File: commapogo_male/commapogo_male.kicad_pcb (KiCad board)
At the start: 2 copper layers, 40.6 x 22.2 mm, 6 parts, among them J1 Conn_02x07_Row_Letter_Last, J2 Conn_02x12_Row_Letter_Last

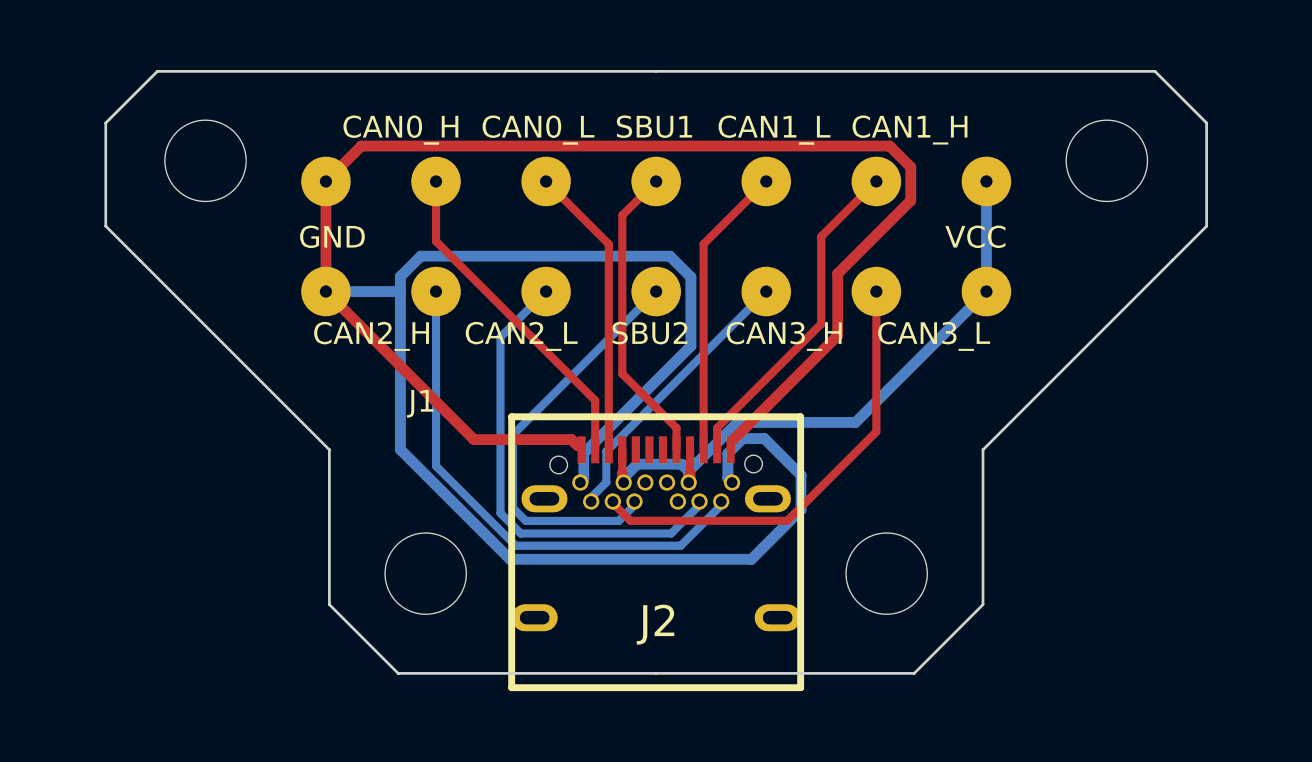
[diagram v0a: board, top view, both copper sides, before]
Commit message: rework usb-c footprint for jlcpcb
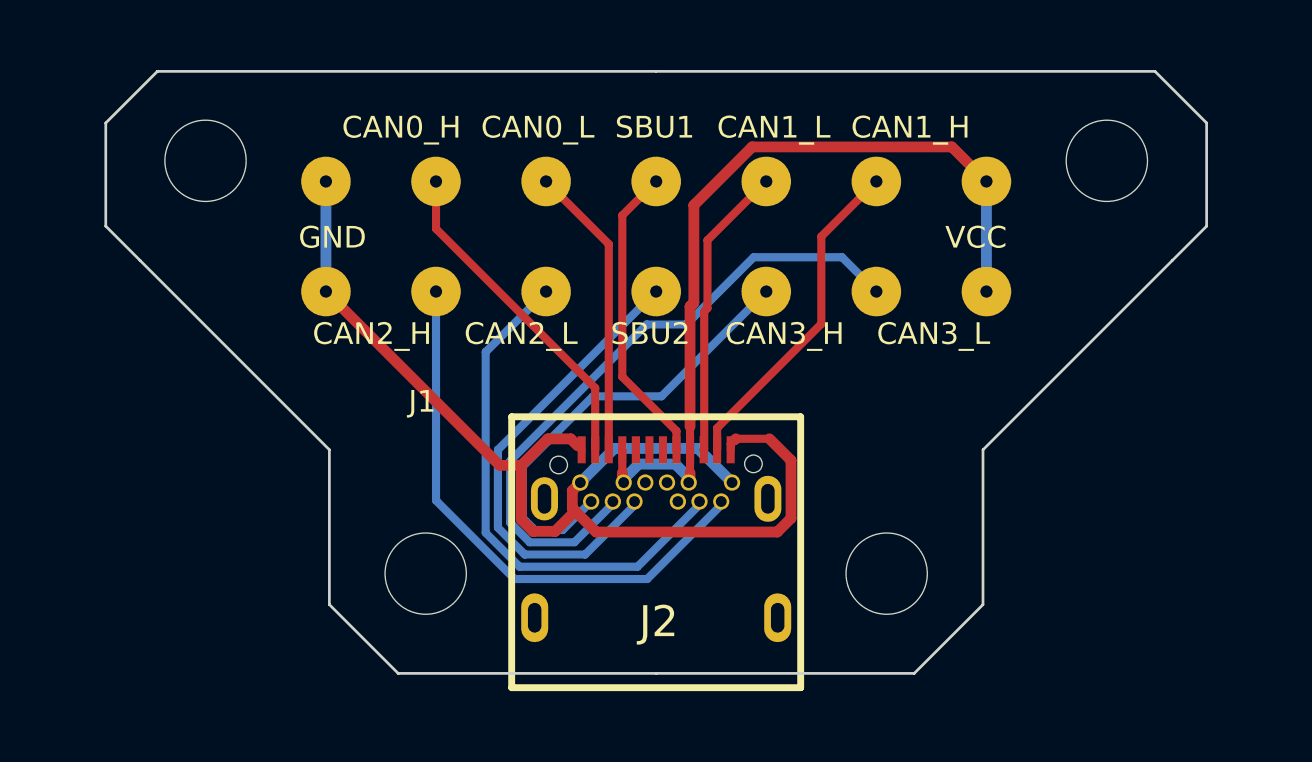
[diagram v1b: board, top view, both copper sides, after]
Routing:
- net GND: track 104.5 -> 42.6 mm
- net /CAN3_L: track 16.6 -> 24.2 mm
- net +12V: track 23.6 -> 31.0 mm
- net /CAN3_H: track 10.4 -> 16.7 mm
- net /SBU2: track 15.2 -> 17.5 mm
- net /CAN2_L: track 17.1 -> 19.3 mm
- net /CAN2_H: track 18.9 -> 20.7 mm

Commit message: revised PCB
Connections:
- J1 pad 10: /CAN2_L -> /CAN3_L
- J1 pad 12: /CAN3_H -> /CAN2_L
- J1 pad 13: /CAN3_L -> /CAN2_H
- J1 pad 7: +12V -> GND
- J1 pad 8: GND -> +12V
- J1 pad 9: /CAN2_H -> /CAN3_H
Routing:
- net /CAN3_L: track 24.2 -> 8.77 mm
- net /SBU2: track 17.5 -> 32.3 mm
- net GND: track 42.6 -> 29.6 mm, vias 0 -> 2
- net /CAN2_L: track 19.3 -> 8.77 mm
- net /CAN2_H: track 20.7 -> 11.0 mm
- net +12V: track 31.0 -> 38.7 mm
- net /CAN3_H: track 16.7 -> 12.7 mm
- added copper zone on B.Cu, net GND
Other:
- board text added: "GND"
- board text added: "VCC"

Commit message: rework pcb design
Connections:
- J2 pad 1: (no net) -> GND
- J2 pad 2: (no net) -> GND
- J2 pad 3: (no net) -> GND
- J2 pad 4: (no net) -> GND
- J2 pad B7: unconnected-(J2-Pin_7b-PadB7) -> /SBU2
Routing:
- net /SBU2: track 32.3 -> 8.21 mm
- net GND: track 29.6 -> 5.61 mm, vias 2 -> 0
- net +12V: track 38.7 -> 35.8 mm
- net /CAN3_H: track 12.7 -> 10.2 mm
- net /CAN2_H: track 11.0 -> 12.7 mm
- net /SBU1: track 11.2 -> 11.6 mm, vias 0 -> 1
- net /CAN1_L: track 10.9 -> 11.1 mm, vias 0 -> 1
- net /CAN0_L: vias 0 -> 1
- net /CAN1_H: vias 0 -> 1
- net /CAN0_H: vias 0 -> 1
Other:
- copper layers 2 -> 4

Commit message: redo pcb design add more ground planes
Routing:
- added copper zone on F.Cu, net GND
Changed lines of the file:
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@@
   (segment (start 138.085 88.585406) (end 138.085 89.39) (width 0.3) (layer "In2.Cu") (net 17))
   (segment (start 132.207 82.707406) (end 132.207 81.788) (width 0.3) (layer "In2.Cu") (net 17))
+  (zone (net 4) (net_name "GND") (layer "F.Cu") (hatch edge 0.5)
+    (priority 1)
+    (connect_pads (clearance 0.5))
+    (min_thickness 0.25) (filled_areas_thickness no)
+    (fill yes (thermal_gap 0.5) (thermal_bridge_width 0.5))
+    (polygon
+      (pts
+        (xy 118.11 73.025)
+        (xy 162.56 73.025)
+        (xy 162.56 97.155)
+        (xy 118.11 97.155)
+      )
+    )
+  )
   (zone locked (net 4) (net_name "GND") (layer "B.Cu") (hatch edge 0.5)
     (connect_pads (clearance 0.5))
